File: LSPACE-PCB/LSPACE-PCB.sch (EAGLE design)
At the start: 5 parts, among them U1 ATSAMD21E17A-AUT, U2 BMI085, U3 AMS_AS7341-DLGMAMS_AS7341-DLG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, U4 RFM95W-868S2, U5 W25Q32FV

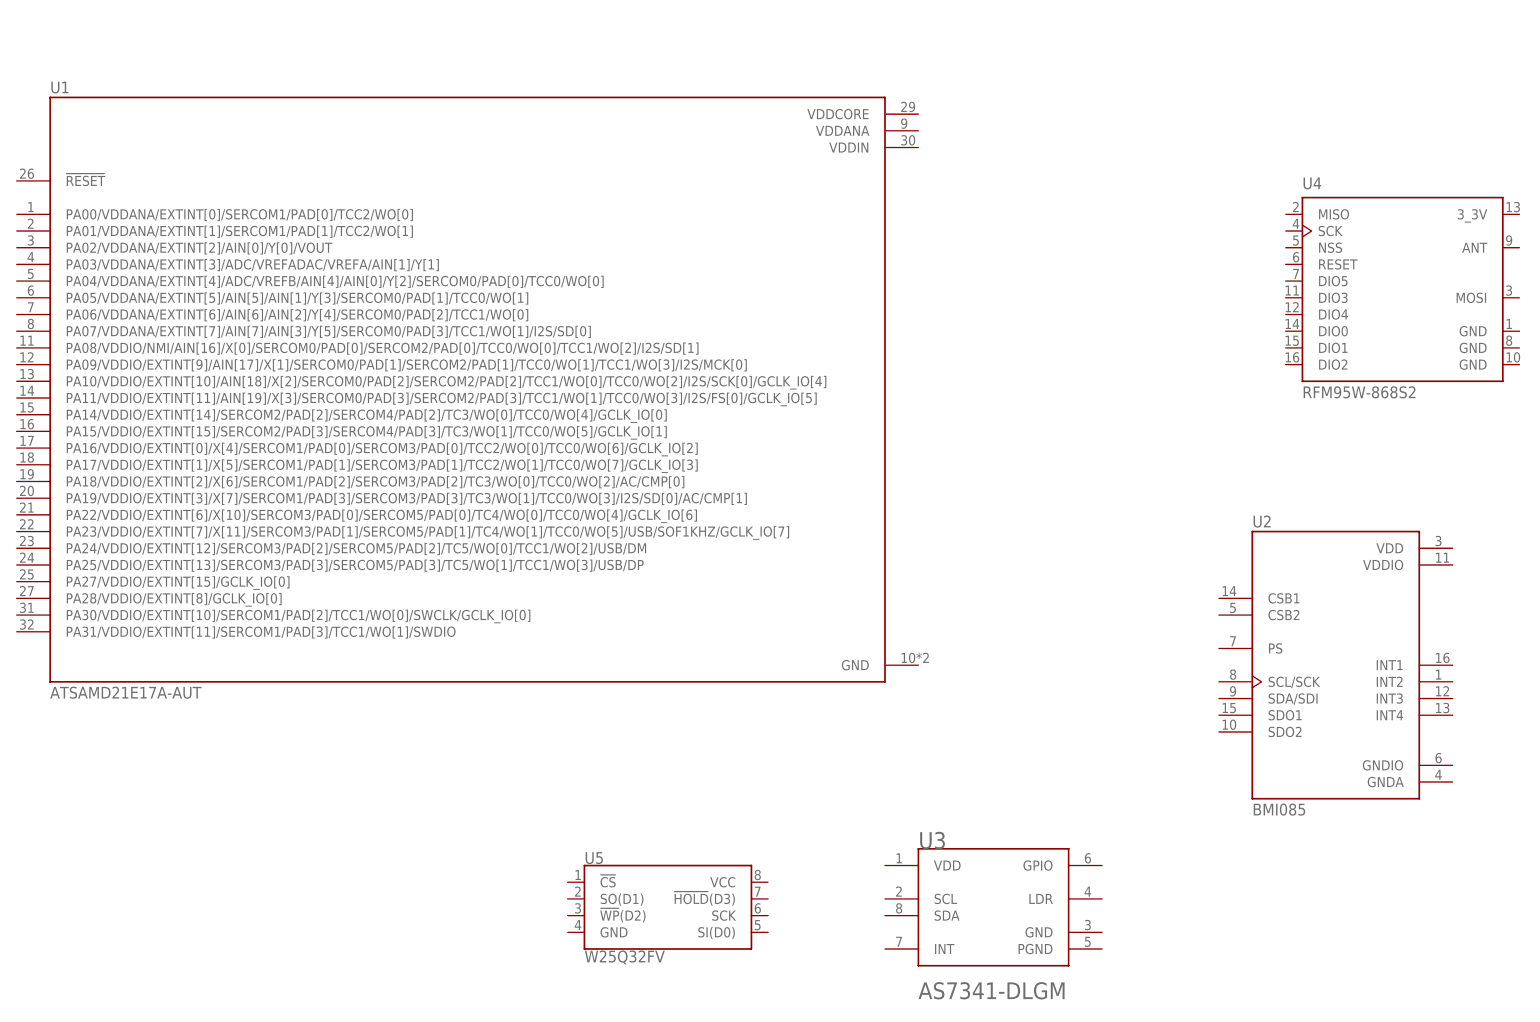
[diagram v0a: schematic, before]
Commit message: Switched to Adafruit based system
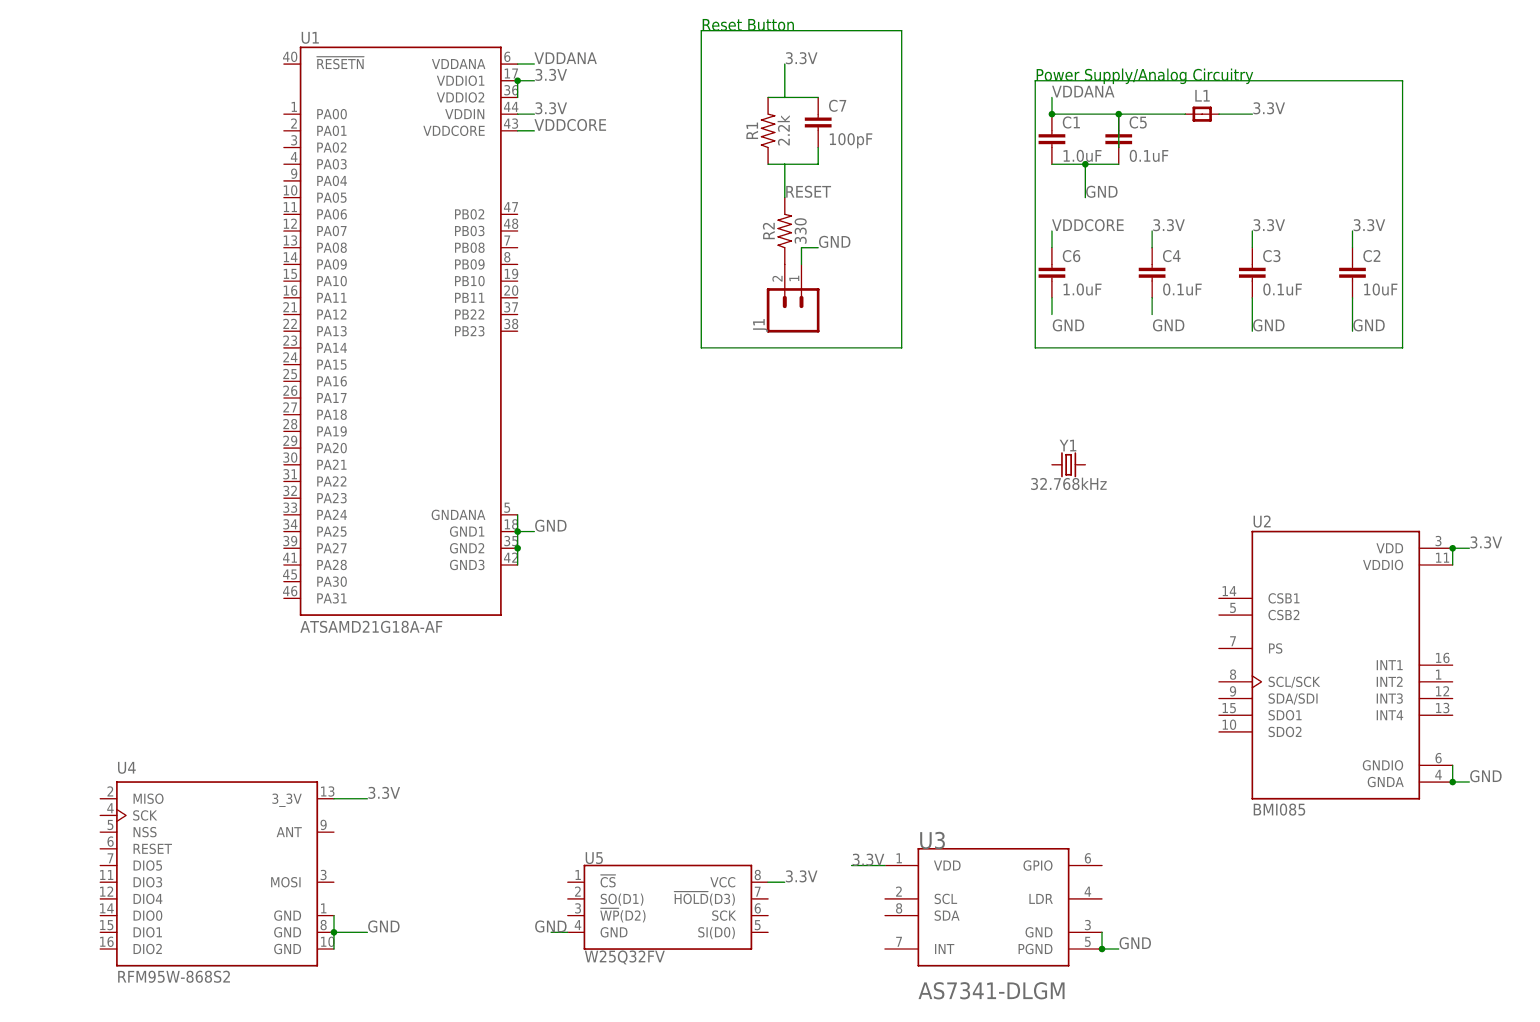
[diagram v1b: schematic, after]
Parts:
- added C1, C6: 1.0uF, SparkFun-Capacitors:1.0UF-1206-50V-10%
- added C2: 10uF, SparkFun-Capacitors:10UF-1206-6.3V-20%
- added C3, C4, C5: 0.1uF, SparkFun-Capacitors:0.1UF-0603-100V-10%
- added C7: 100pF, SparkFun-Capacitors:100PF-0603-50V-5%
- added J1: (no value), SparkFun-Connectors:CONN_02
- added L1: (no value), 52101-101-REV-A_v16:RC-MASTER-SMD_FB_1206MP
- added R1: 2.2k, SparkFun-Resistors:2.2KOHM-0603-1/10W-1%
- added R2: 330, SparkFun-Resistors:330OHM-0603-1/10W-1%
- added Y1: 32.768kHz, SparkFun-Clocks:CRYSTAL-32.768KHZSMD-3.2X1.5
- U1: value ATSAMD21E17A-AUT -> ATSAMD21G18A-AF; device ATSAMD21E17A-AUT:ATSAMD21E17A-AUT -> ATSAMD21G18A-AF:ATSAMD21G18A-AF
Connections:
- new net 3.3V: C2.1, C3.1, C4.1, C7.1, L1.2, R1.2, U1.VDDIN, U1.VDDIO1, U1.VDDIO2, U2.VDD, U2.VDDIO, U3.VDD, U4.3_3V, U5.VCC
- new net GND: C1.2, C2.2, C3.2, C4.2, C5.2, C6.2, J1.1, U1.GND1, U1.GND2, U1.GND3, U1.GNDANA, U2.GNDA, U2.GNDIO, U3.GND, U3.PGND, U4.GND, U4.GND@1, U4.GND@2, U5.GND
- new net N$1: J1.2, R2.1
- new net RESET: C7.2, R1.1, R2.2
- new net VDDANA: C1.1, C5.1, L1.1, U1.VDDANA
- new net VDDCORE: C6.1, U1.VDDCORE
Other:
- note added: "Power Supply/Analog Circuitry"
- note added: "Reset Button"
- moved on the sheet: U4
